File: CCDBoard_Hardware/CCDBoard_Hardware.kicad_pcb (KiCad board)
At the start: 2 copper layers, 50.8 x 21.1 mm, 7 parts, among them U1 TCD1304

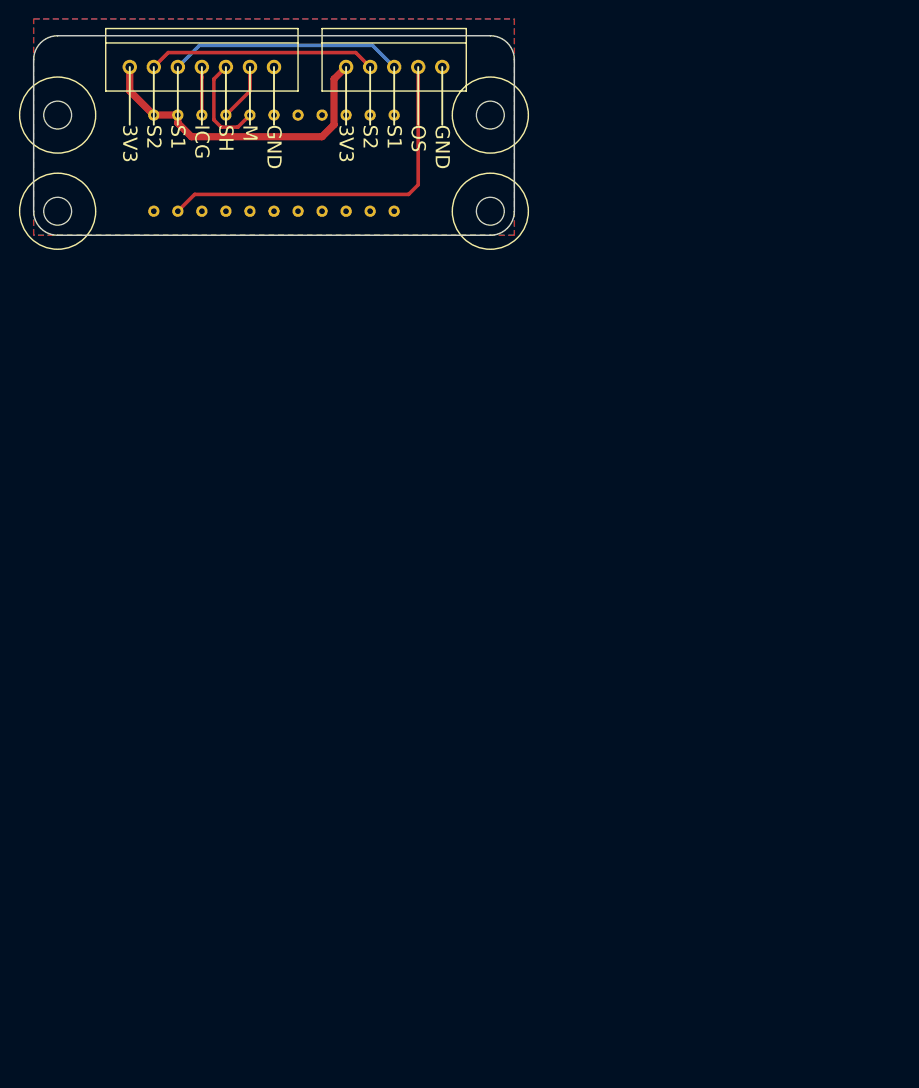
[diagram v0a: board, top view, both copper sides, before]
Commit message: Created new netlist
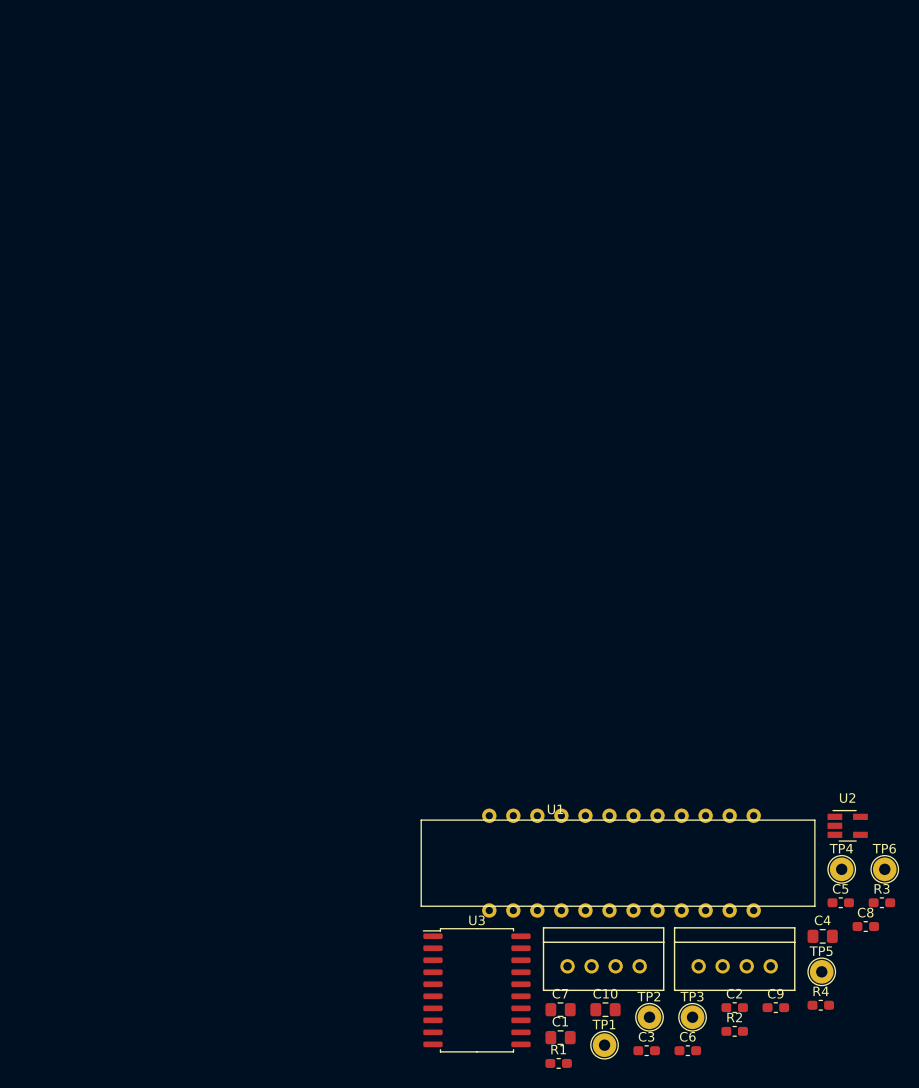
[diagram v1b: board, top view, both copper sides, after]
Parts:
- removed REF** (x4): 4_40_Hole, MRDT_Drill_Holes:4_40_Hole
- added C1: 22 µF/25 V, Capacitor_SMD:C_0805_2012Metric_Pad1.15x1.40mm_HandSolder, F.Cu at (55.7, 84.8)
- added C10: 22 µF/25 V, Capacitor_SMD:C_0805_2012Metric_Pad1.15x1.40mm_HandSolder, F.Cu at (60.4, 81.8)
- added C2: 0.1 µF, Capacitor_SMD:C_0603_1608Metric_Pad1.05x0.95mm_HandSolder, F.Cu at (74.1, 81.6)
- added C3: 0.1 µF, Capacitor_SMD:C_0603_1608Metric_Pad1.05x0.95mm_HandSolder, F.Cu at (64.8, 86.2)
- added C4: 22 µF/25 V, Capacitor_SMD:C_0805_2012Metric_Pad1.15x1.40mm_HandSolder, F.Cu at (83.4, 74.1)
- added C5: 1 µF, Capacitor_SMD:C_0603_1608Metric_Pad1.05x0.95mm_HandSolder, F.Cu at (85.3, 70.5)
- added C6: 0.1 µF, Capacitor_SMD:C_0603_1608Metric_Pad1.05x0.95mm_HandSolder, F.Cu at (69.1, 86.2)
- added C7: 22 µF/25 V, Capacitor_SMD:C_0805_2012Metric_Pad1.15x1.40mm_HandSolder, F.Cu at (55.7, 81.8)
- added C8: 22 pF, Capacitor_SMD:C_0603_1608Metric_Pad1.05x0.95mm_HandSolder, F.Cu at (87.9, 73.0)
- added C9: 0.1 µF, Capacitor_SMD:C_0603_1608Metric_Pad1.05x0.95mm_HandSolder, F.Cu at (78.4, 81.6)
- added R1: 82 Ω, Resistor_SMD:R_0603_1608Metric_Pad1.05x0.95mm_HandSolder, F.Cu at (55.5, 87.5)
- added R2: 82 Ω, Resistor_SMD:R_0603_1608Metric_Pad1.05x0.95mm_HandSolder, F.Cu at (74.1, 84.1)
- added R3: 100 Ω, Resistor_SMD:R_0603_1608Metric_Pad1.05x0.95mm_HandSolder, F.Cu at (89.6, 70.5)
- added R4: 51 Ω, Resistor_SMD:R_0603_1608Metric_Pad1.05x0.95mm_HandSolder, F.Cu at (83.2, 81.4)
- added TP1: VideoTestPoint, TestPoint:TestPoint_THTPad_D2.5mm_Drill1.2mm, F.Cu at (60.3, 85.6)
- added TP2: TrigTestPoint, TestPoint:TestPoint_THTPad_D2.5mm_Drill1.2mm, F.Cu at (65.1, 82.6)
- added TP3: EOSTestPoint, TestPoint:TestPoint_THTPad_D2.5mm_Drill1.2mm, F.Cu at (69.6, 82.6)
- added TP4: VideoPreAmpTestPoint, TestPoint:TestPoint_THTPad_D2.5mm_Drill1.2mm, F.Cu at (85.4, 67.0)
- added TP5: CLKTestPoint, TestPoint:TestPoint_THTPad_D2.5mm_Drill1.2mm, F.Cu at (83.3, 77.8)
- added TP6: STTestPoint, TestPoint:TestPoint_THTPad_D2.5mm_Drill1.2mm, F.Cu at (89.9, 67.0)
- added U2: LT1818, Package_TO_SOT_SMD:SOT-23-5_HandSoldering, F.Cu at (86.0, 62.4)
- added U3: 74HC541, Package_SO:SOIC-20W_7.5x12.8mm_P1.27mm, F.Cu at (46.8, 79.8)
- Conn1: value Molex_SL_05 -> Molex_SL_04 IN; footprint MRDT_Connectors:MOLEX_SL_05_Vertical -> MRDT_Connectors:MOLEX_SL_04_Vertical
- Conn2: value Molex_SL_07 -> Molex_SL_04 OUT; footprint MRDT_Connectors:MOLEX_SL_07_Vertical -> MRDT_Connectors:MOLEX_SL_04_Vertical
- U1: value TCD1304 -> S11639-01; footprint MRDT_Sensors:TCD-1304 -> MRDT_Devices:CCD-S11639-01; moved to F.Cu
- moved Conn2 110.5 mm to (74.1, 77.2)
- moved U1 109.8 mm to (76.1, 70.9), turned to 0 degrees
- moved Conn1 97.6 mm to (60.2, 77.2)
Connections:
- Conn1 pad 1: +3V3 -> +5V
- Conn1 pad 2: Sync2 -> ST
- Conn1 pad 3: Sync1 -> CLK
- Conn1 pad 4: OS -> GND
- Conn2 pad 1: +3V3 -> Trig
- Conn2 pad 2: Sync2 -> EOS
- Conn2 pad 3: Sync1 -> Video
- Conn2 pad 4: ICG -> GND
- U1 pad 1: +3V3 -> (no net)
- U1 pad 2: +3V3 -> (no net)
- U1 pad 21: OS -> (no net)
- U1 pad 22: GND -> (no net)
- U1 pad 3: ICG -> (no net)
- U1 pad 4: M -> (no net)
- U1 pad 5: SH -> (no net)
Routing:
- net OS: track 39.0 -> 0.00 mm
- net +3V3: track 33.8 -> 0.00 mm
- net Sync1: track 24.8 -> 0.00 mm
- net Sync2: track 24.1 -> 0.00 mm
- net SH: track 10.8 -> 0.00 mm
- net M: track 6.13 -> 0.00 mm
- net ICG: track 5.08 -> 0.00 mm
- removed copper zone on B.Cu, net GND
- removed copper zone on F.Cu, net GND
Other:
- board outline removed
- board text removed: "3V3"
- board text removed: "CCDBoard Hardware, Rev 1 Mars Rover Design Team Missouri S&T, 2019 Andrew Van Horn"
- board text removed: "GND"
- board text removed: "ICG"
- board text removed: "M"
- board text removed: "OS"
- board text removed: "S1"
- board text removed: "S2"
- board text removed: "SH"

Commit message: maybe
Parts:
- moved TP1 124.7 mm to (171.6, 29.2)
- moved C10 118.9 mm to (179.1, 74.4), turned to 90 degrees
- moved C7 115.7 mm to (164.3, 42.2), turned to 90 degrees
- moved Conn2 107.9 mm to (167.1, 22.6)
- moved C6 101.0 mm to (160.0, 42.1), turned to 90 degrees
- moved U3 100.7 mm to (139.1, 39.4), turned to 90 degrees
- moved R4 99.4 mm to (172.0, 36.6), turned to 270 degrees
- moved C1 98.2 mm to (131.3, 22.1)
- moved C8 97.1 mm to (176.3, 32.8), turned to 270 degrees
- moved C9 96.3 mm to (174.5, 74.3), turned to 90 degrees
- moved U1 96.2 mm to (172.2, 66.7)
- moved R1 94.7 mm to (149.2, 73.9), turned to 90 degrees
- moved TP2 89.3 mm to (137.2, 29.8)
- moved TP3 88.7 mm to (141.0, 29.8)
- moved TP4 88.0 mm to (172.2, 52.7)
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
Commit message: connected testpoints
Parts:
- moved TP1 53.6 mm to (123.7, 53.3)
- moved Conn2 41.5 mm to (127.5, 35.1)
- moved U3 32.6 mm to (116.3, 62.7)
- moved TP6 24.9 mm to (113.3, 41.7)
- moved TP3 24.7 mm to (123.7, 47.5)
- moved Conn1 22.7 mm to (114.6, 35.1), turned to 0 degrees
- moved TP5 20.1 mm to (113.3, 47.5)
- moved TP2 17.9 mm to (123.7, 41.7)
- moved C2 5.85 mm to (131.1, 20.6)
- moved C1 5.85 mm to (131.1, 16.3)
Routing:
- net Video: track 0.00 -> 20.4 mm
- net EOS: track 0.00 -> 13.5 mm
- net CLK: track 0.00 -> 13.5 mm
- net Trig: track 0.00 -> 6.60 mm
- net ST: track 0.00 -> 6.60 mm
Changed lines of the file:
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@@
     (thickness 1.6)
     (drawings 0)
-    (tracks 0)
+    (tracks 8)
     (zones 0)
     (modules 25)
@@
   )
   (module Capacitor_SMD:C_0805_2012Metric_Pad1.15x1.40mm_HandSolder (layer F.Cu)
-    (at 131.309 22.098)
+    (at 131.055 16.256)
     (descr "Capacitor SMD 0805 (2012 Metric), square (rectangular) end terminal, IPC_7351 nominal with elongated pad for handsoldering. (Body size source: https://docs.google.com/spreadsheets/d/1BsfQQcO9C6DZCsRaXUlFlo91Tg2WpOkGARC1WS5S8t0/edit?usp=sharing), generated with kicad-footprint-generator")
     (tags "capacitor handsolder")
@@
   )
   (module Capacitor_SMD:C_0603_1608Metric_Pad1.05x0.95mm_HandSolder (layer F.Cu)
-    (at 131.318 26.416)
+    (at 131.064 20.574)
     (descr "Capacitor SMD 0603 (1608 Metric), square (rectangular) end terminal, IPC_7351 nominal with elongated pad for handsoldering. (Body size source: http://www.tortai-tech.com/upload/download/2011102023233369053.pdf), generated with kicad-footprint-generator")
     (tags "capacitor handsolder")
@@
   )
   (module MRDT_Connectors:MOLEX_SL_04_Vertical (layer F.Cu)
-    (at 114.935 57.785 90)
-    (fp_text reference Conn1 (at -4.445 3.302 90) (layer F.SilkS) hide
-      (effects (font (size 1 1) (thickness 0.15)))
-    )
-    (fp_text value "Molex_SL_04 IN" (at -0.254 3.302 90) (layer F.Fab)
+    (at 114.554 35.052)
+    (fp_text reference Conn1 (at -4.445 3.302) (layer F.SilkS) hide
+      (effects (font (size 1 1) (thickness 0.15)))
+    )
+    (fp_text value "Molex_SL_04 IN" (at -0.254 3.302) (layer F.Fab)
       (effects (font (size 1 1) (thickness 0.15)))
     )
@@
     (fp_line (start 6.35 -2.54) (end 6.35 -4.064) (layer F.SilkS) (width 0.15))
     (fp_line (start 6.35 -4.064) (end -6.35 -4.064) (layer F.SilkS) (width 0.15))
-    (pad 4 thru_hole circle (at 3.81 0 90) (size 1.524 1.524) (drill 0.9) (layers *.Cu *.Mask)
-      (net 1 GND))
-    (pad 4 thru_hole circle (at 3.81 0 90) (size 1.524 1.524) (drill 0.9) (layers *.Cu *.Mask)
-      (net 1 GND))
-    (pad 3 thru_hole circle (at 1.27 0 90) (size 1.524 1.524) (drill 0.9) (layers *.Cu *.Mask)
+    (pad 4 thru_hole circle (at 3.81 0) (size 1.524 1.524) (drill 0.9) (layers *.Cu *.Mask)
+      (net 1 GND))
+    (pad 4 thru_hole circle (at 3.81 0) (size 1.524 1.524) (drill 0.9) (layers *.Cu *.Mask)
+      (net 1 GND))
+    (pad 3 thru_hole circle (at 1.27 0) (size 1.524 1.524) (drill 0.9) (layers *.Cu *.Mask)
       (net 5 CLK))
-    (pad 2 thru_hole circle (at -1.27 0 90) (size 1.524 1.524) (drill 0.9) (layers *.Cu *.Mask)
+    (pad 2 thru_hole circle (at -1.27 0) (size 1.524 1.524) (drill 0.9) (layers *.Cu *.Mask)
       (net 6 ST))
-    (pad 1 thru_hole circle (at -3.81 0 90) (size 1.524 1.524) (drill 0.9) (layers *.Cu *.Mask)
+    (pad 1 thru_hole circle (at -3.81 0) (size 1.524 1.524) (drill 0.9) (layers *.Cu *.Mask)
       (net 2 +5V))
     (model "${MRDT_KICAD_LIBRARIES}/3D Files/MRDT_Connctors/Molex_SL_04_Vertical.stp"
@@
   )
   (module MRDT_Connectors:MOLEX_SL_04_Vertical (layer F.Cu)
-    (at 167.132 22.606)
+    (at 127.508 35.052)
     (fp_text reference Conn2 (at -4.445 3.302) (layer F.SilkS) hide
       (effects (font (size 1 1) (thickness 0.15)))
@@
   )
   (module TestPoint:TestPoint_THTPad_D2.5mm_Drill1.2mm (layer F.Cu)
-    (at 171.577 29.21)
+    (at 123.698 53.34)
     (descr "THT pad as test Point, diameter 2.5mm, hole diameter 1.2mm ")
     (tags "test point THT pad")
@@
   )
   (module TestPoint:TestPoint_THTPad_D2.5mm_Drill1.2mm (layer F.Cu)
-    (at 137.16 29.845)
+    (at 123.698 41.656)
     (descr "THT pad as test Point, diameter 2.5mm, hole diameter 1.2mm ")
     (tags "test point THT pad")
@@
   )
   (module TestPoint:TestPoint_THTPad_D2.5mm_Drill1.2mm (layer F.Cu)
-    (at 140.97 29.845)
+    (at 123.698 47.498)
     (descr "THT pad as test Point, diameter 2.5mm, hole diameter 1.2mm ")
     (tags "test point THT pad")
@@
   )
   (module TestPoint:TestPoint_THTPad_D2.5mm_Drill1.2mm (layer F.Cu)
-    (at 133.35 48.895)
+    (at 113.284 47.498)
     (descr "THT pad as test Point, diameter 2.5mm, hole diameter 1.2mm ")
     (tags "test point THT pad")
@@
   )
   (module TestPoint:TestPoint_THTPad_D2.5mm_Drill1.2mm (layer F.Cu)
-    (at 137.16 48.895)
+    (at 113.284 41.656)
     (descr "THT pad as test Point, diameter 2.5mm, hole diameter 1.2mm ")
     (tags "test point THT pad")
@@
   )
   (module Package_SO:SOIC-20W_7.5x12.8mm_P1.27mm (layer F.Cu)
-    (at 139.065 39.37 90)
+    (at 116.332 62.738 90)
     (descr "SOIC, 20 Pin (JEDEC MS-013AC, https://www.analog.com/media/en/package-pcb-resources/package/233848rw_20.pdf), generated with kicad-footprint-generator ipc_gullwing_generator.py")
     (tags "SOIC SO")
@@
     )
   )
+  (segment (start 128.778 48.26) (end 128.778 35.052) (width 0.25) (layer F.Cu) (net 4))
+  (segment (start 123.698 53.34) (end 128.778 48.26) (width 0.25) (layer F.Cu) (net 4))
+  (segment (start 115.824 44.958) (end 115.824 35.052) (width 0.25) (layer F.Cu) (net 5))
+  (segment (start 113.284 47.498) (end 115.824 44.958) (width 0.25) (layer F.Cu) (net 5))
+  (segment (start 113.284 41.656) (end 113.284 35.052) (width 0.25) (layer F.Cu) (net 6))
+  (segment (start 123.698 41.656) (end 123.698 35.052) (width 0.25) (layer F.Cu) (net 7))
+  (segment (start 126.238 44.958) (end 126.238 35.052) (width 0.25) (layer F.Cu) (net 8))
+  (segment (start 123.698 47.498) (end 126.238 44.958) (width 0.25) (layer F.Cu) (net 8))
 )

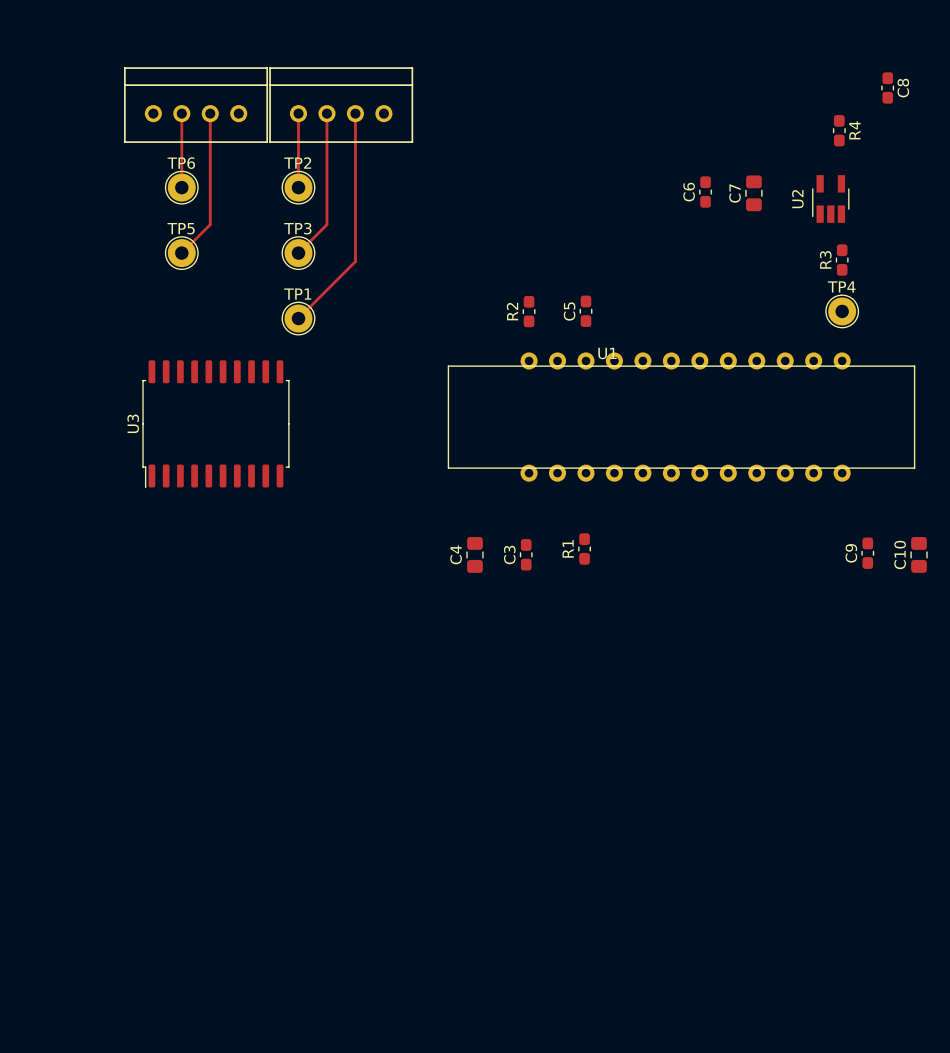
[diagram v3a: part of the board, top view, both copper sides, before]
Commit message: Ratsnest is accurate follow it
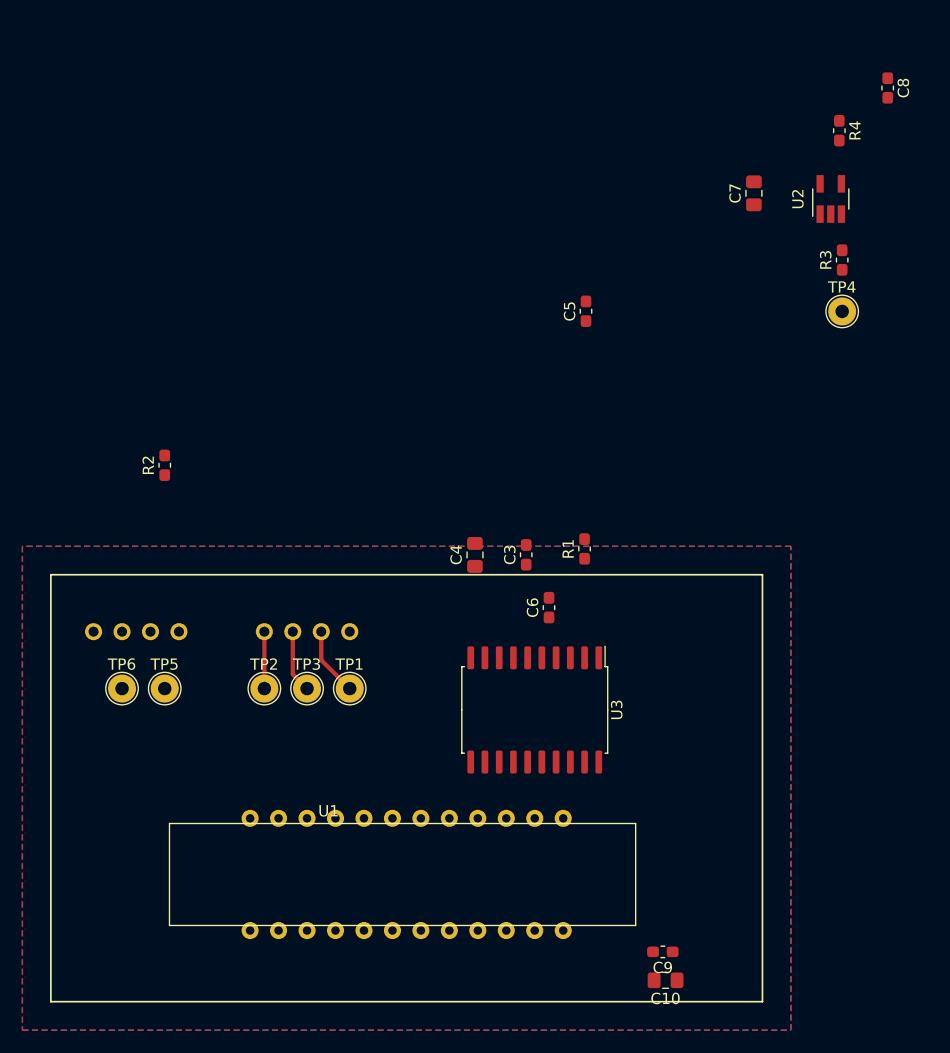
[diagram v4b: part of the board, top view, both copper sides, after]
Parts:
- Conn1, Conn2: moved to B.Cu
- moved U1 47.8 mm to (147.3, 107.5)
- moved Conn1 46.5 mm to (109.2, 81.3), turned to 180 degrees
- moved Conn2 46.3 mm to (124.5, 81.3), turned to 180 degrees
- moved TP6 45.0 mm to (108.0, 86.4)
- moved TP2 44.8 mm to (120.7, 86.4)
- moved C10 44.2 mm to (156.5, 112.4), turned to 180 degrees
- moved C9 40.0 mm to (156.2, 109.9), turned to 180 degrees
- moved C6 39.6 mm to (146.1, 79.1)
- moved TP5 38.9 mm to (111.8, 86.4)
- moved TP3 38.9 mm to (124.5, 86.4)
- moved U3 38.2 mm to (144.8, 88.3), turned to 270 degrees
- moved R2 35.3 mm to (111.8, 66.4)
- moved TP1 33.3 mm to (128.3, 86.4)
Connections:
- U1 pad 1: (no net) -> +5V
- U1 pad 10: (no net) -> Net-(U1-Pad10)
- U1 pad 11: (no net) -> GND
- U1 pad 12: (no net) -> +5V
- U1 pad 13: (no net) -> Net-(R3-Pad2)
- U1 pad 14: (no net) -> Net-(U1-Pad14)
- U1 pad 15: (no net) -> EOS_OUT
- U1 pad 16: (no net) -> Net-(U1-Pad16)
- U1 pad 17: (no net) -> Net-(U1-Pad17)
- U1 pad 18: (no net) -> Net-(U1-Pad18)
- U1 pad 19: (no net) -> Net-(U1-Pad19)
- U1 pad 2: (no net) -> GND
- U1 pad 20: (no net) -> Net-(U1-Pad20)
- U1 pad 21: (no net) -> Net-(U1-Pad21)
- U1 pad 22: (no net) -> Net-(C5-Pad1)
- U1 pad 23: (no net) -> Trig_OUT
- U1 pad 24: (no net) -> Net-(R2-Pad2)
- U1 pad 3: (no net) -> Net-(R1-Pad1)
- U1 pad 4: (no net) -> Net-(U1-Pad4)
- U1 pad 5: (no net) -> Net-(U1-Pad5)
- U1 pad 6: (no net) -> Net-(U1-Pad6)
- U1 pad 7: (no net) -> Net-(U1-Pad7)
- U1 pad 8: (no net) -> Net-(U1-Pad8)
- U1 pad 9: (no net) -> Net-(U1-Pad9)
- U3 pad 1: (no net) -> Net-(U3-Pad1)
- U3 pad 10: (no net) -> GND
- U3 pad 11: (no net) -> Net-(U3-Pad11)
- U3 pad 12: (no net) -> Net-(U3-Pad12)
- U3 pad 13: (no net) -> Net-(U3-Pad13)
- U3 pad 14: (no net) -> Net-(U3-Pad14)
- U3 pad 15: (no net) -> EOS
- U3 pad 16: (no net) -> Trig
- U3 pad 17: (no net) -> CLK_IN
- U3 pad 18: (no net) -> ST_IN
- U3 pad 19: (no net) -> Net-(U3-Pad19)
- U3 pad 2: (no net) -> ST
- U3 pad 20: (no net) -> +5V
- U3 pad 3: (no net) -> CLK
- U3 pad 4: (no net) -> Trig_OUT
- U3 pad 5: (no net) -> EOS_OUT
- U3 pad 6: (no net) -> Net-(U3-Pad6)
- U3 pad 7: (no net) -> Net-(U3-Pad7)
- U3 pad 8: (no net) -> Net-(U3-Pad8)
- U3 pad 9: (no net) -> Net-(U3-Pad9)
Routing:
- net Video: track 20.4 -> 6.13 mm
- net CLK: track 13.5 -> 0.00 mm
- net EOS: track 13.5 -> 5.61 mm
- net ST: track 6.60 -> 0.00 mm
- net Trig: track 6.60 -> 5.08 mm
- added copper zone on F.Cu, net +5V
- added copper zone on B.Cu, net GND

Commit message: needs reformat
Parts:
- removed C7: 22 µF/25 V, Capacitor_SMD:C_0805_2012Metric_Pad1.15x1.40mm_HandSolder
- moved C1 64.0 mm to (133.3, 80.3), turned to 270 degrees
- moved C2 59.6 mm to (135.9, 80.0), turned to 270 degrees
- moved R4 52.5 mm to (161.3, 88.0), turned to 90 degrees
- moved C8 52.2 mm to (160.4, 82.5), turned to 180 degrees
- moved TP4 47.4 mm to (157.5, 97.8)
- moved R3 47.3 mm to (157.5, 93.1), turned to 270 degrees
- moved U2 46.8 mm to (157.8, 87.5)
- moved R1 44.8 mm to (125.3, 111.8), turned to 0 degrees
- moved C5 29.4 mm to (138.4, 80.0), turned to 270 degrees
- moved R2 28.6 mm to (119.4, 94.0), turned to 270 degrees
- moved C3 11.6 mm to (153.7, 80.9), turned to 270 degrees
- moved C6 10.3 mm to (156.2, 80.9), turned to 270 degrees
- moved TP1 7.62 mm to (120.7, 86.4)
- moved TP2 7.62 mm to (128.3, 86.4)
- moved C4 6.02 mm to (142.2, 79.8), turned to 270 degrees
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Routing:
- net GND: track 0.00 -> 65.2 mm
- net CLK: track 0.00 -> 54.3 mm, vias 0 -> 2
- net ST: track 0.00 -> 49.8 mm, vias 0 -> 2
- net EOS: track 5.61 -> 41.5 mm, vias 0 -> 2
- net CLK_IN: track 0.00 -> 35.5 mm
- net Trig_OUT: track 0.00 -> 32.0 mm, vias 0 -> 2
- net ST_IN: track 0.00 -> 30.4 mm, vias 0 -> 2
- net Net-(C5-Pad1): track 0.00 -> 25.9 mm, vias 0 -> 2
- net EOS_OUT: track 0.00 -> 18.8 mm
- net Net-(R3-Pad2): track 0.00 -> 14.0 mm
- net Video: track 6.13 -> 10.7 mm
- net +5V: track 0.00 -> 3.87 mm
- net Net-(R1-Pad1): track 0.00 -> 3.81 mm
- net Net-(R3-Pad1): track 0.00 -> 3.59 mm
- net Net-(R4-Pad1): track 0.00 -> 3.49 mm
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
